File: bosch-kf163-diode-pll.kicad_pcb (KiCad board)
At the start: 2 copper layers, 19 x 36.8 mm, 49 parts, among them U1 PLL

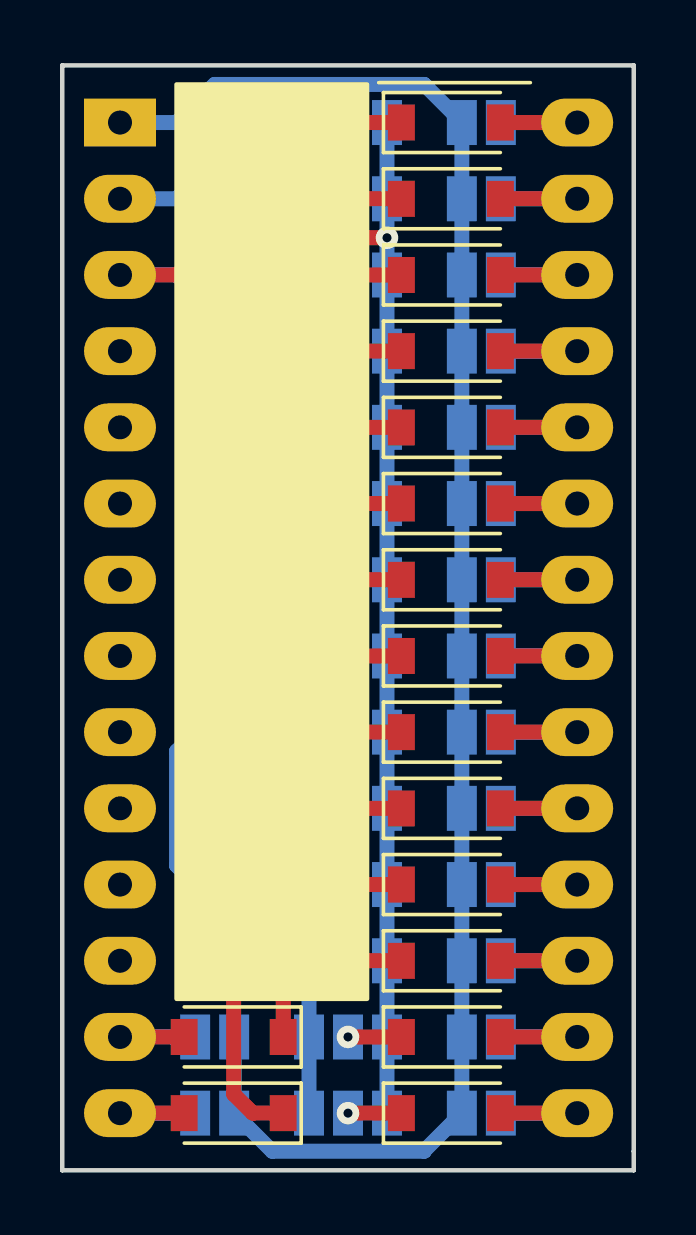
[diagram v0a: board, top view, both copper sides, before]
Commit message: changed to smaller diodes, added schematic pdf and gerbers
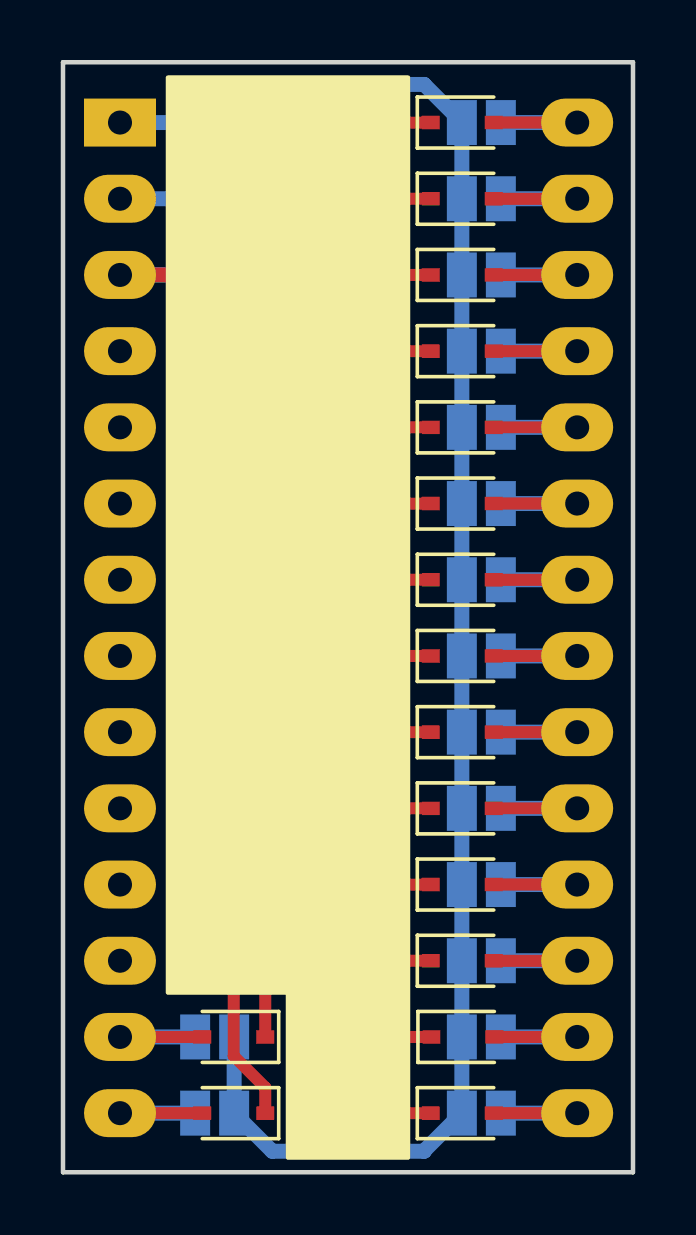
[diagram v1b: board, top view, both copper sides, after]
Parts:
- D1, D10, D11, D12, D13, D14, D15, D16, D2, D3, D4, D5, D6, D7, D8, D9: footprint Diode_SMD:D_SOD-123 -> Diode_SMD:D_SOD-323
- moved D13 0.40 mm to (129.6, 96.5)
- moved D1 0.38 mm to (129.5, 66.0)
- moved D10 0.38 mm to (129.5, 88.9)
- moved D11 0.38 mm to (129.5, 91.4)
- moved D12 0.38 mm to (129.5, 94.0)
- moved D14 0.38 mm to (129.5, 99.1)
- moved D2 0.38 mm to (129.5, 68.6)
- moved D3 0.38 mm to (129.5, 71.1)
- moved D4 0.38 mm to (129.5, 73.7)
- moved D5 0.38 mm to (129.5, 76.2)
- moved D6 0.38 mm to (129.5, 78.7)
- moved D7 0.38 mm to (129.5, 81.3)
- moved D8 0.38 mm to (129.5, 83.8)
- moved D9 0.38 mm to (129.5, 86.4)
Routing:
- net Net-(D13-Pad1): track 1.78 -> 2.78 mm
- net Net-(D9-Pad1): track 1.78 -> 2.76 mm
- net Net-(D8-Pad1): track 1.78 -> 2.76 mm
- net Net-(D7-Pad1): track 1.78 -> 2.76 mm
- net Net-(D6-Pad1): track 1.78 -> 2.76 mm
- net Net-(D5-Pad1): track 1.78 -> 2.76 mm
- net Net-(D4-Pad1): track 1.78 -> 2.76 mm
- net Net-(D3-Pad1): track 1.78 -> 2.76 mm
- net Net-(D2-Pad1): track 1.78 -> 2.76 mm
- net Net-(D14-Pad1): track 1.78 -> 2.76 mm
- net Net-(D12-Pad1): track 1.78 -> 2.76 mm
- net Net-(D11-Pad1): track 1.78 -> 2.76 mm
- net Net-(D10-Pad1): track 1.78 -> 2.76 mm
- net Net-(D1-Pad1): track 1.78 -> 2.76 mm
- net Net-(D15-Pad1): track 7.63 -> 6.78 mm
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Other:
- board size 19 x 36.8 mm -> 19 x 37 mm
- board text added: "RobinOlejnik.com"
- board text removed: "RobinOlejnik.de"
